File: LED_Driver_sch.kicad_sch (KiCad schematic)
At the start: 32 parts, among them J7 12V IN, J8 12V RGB LED, Q1 PMOS, Q2 NMOS, Q3 NMOS, Q4 NMOS, U6 TLV9001TIDCKR

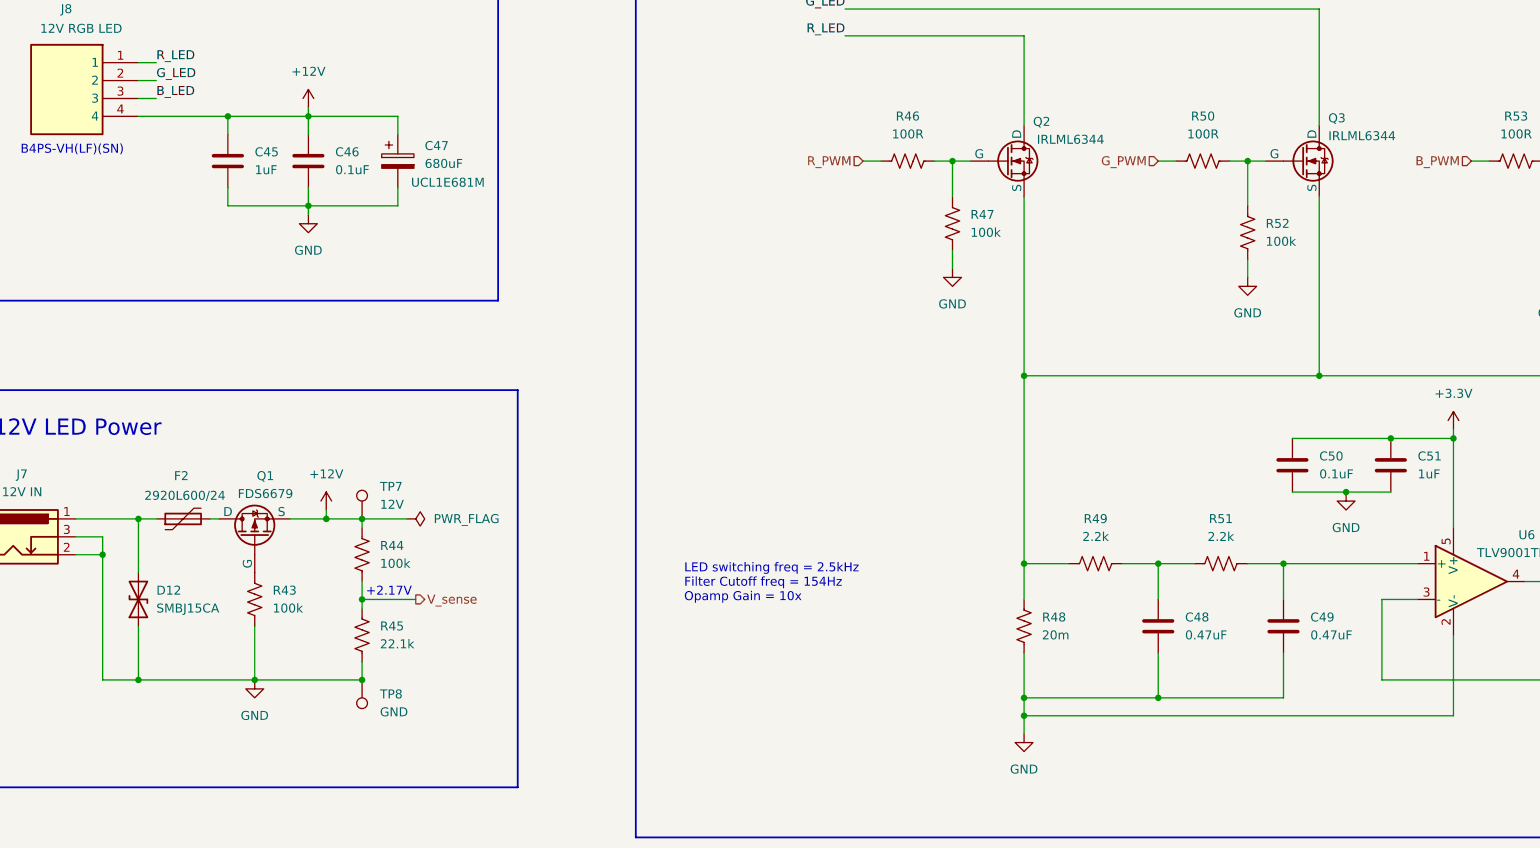
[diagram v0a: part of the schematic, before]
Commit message: Alternate MPNs added
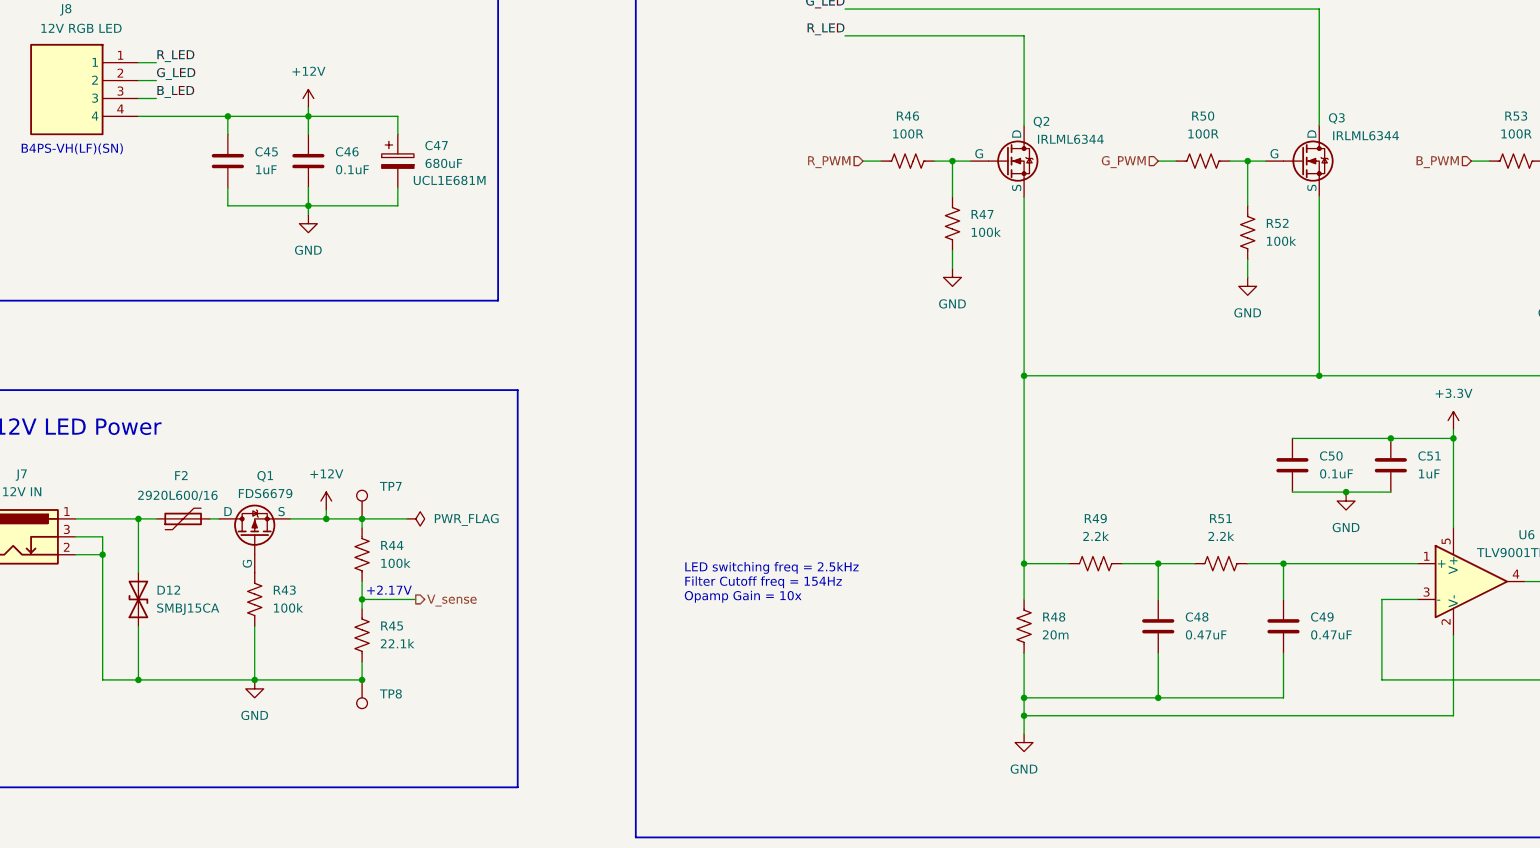
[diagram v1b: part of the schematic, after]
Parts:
- C46: MPN GRM188R71H104KA93D -> C0603C104K5RACTU
- C47: MPN UCL1E681M -> UCL1E681MNL1GS; Manufacturer_Part_Number (none) -> UCL1E681M
- F2: MPN 2920L600/24 -> 2920L600/16MR; Manufacturer_Part_Number (none) -> 2920L600/16
- Q1: MPN FDS6679 -> FDS6679AZ; Manufacturer_Part_Number (none) -> FDS6679
- Q2, Q3, Q4: MPN IRLML6344 -> IRLML6344TRPBF; Manufacturer_Part_Number (none) -> IRLML6344
- TP7: value 12V -> TestPoint
- TP8: value GND -> TestPoint
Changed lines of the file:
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@@
 			)
 		)
-		(property "MPN" "IRLML6344"
+		(property "MPN" "IRLML6344TRPBF"
 			(at 184.404 62.992 0)
 			(effects
@@
 					(color 0 132 132 1)
 				)
+				(hide yes)
 			)
 		)
-		(property "Manufacturer_Part_Number" ""
-			(at 175.26 66.04 0)
+		(property "Manufacturer_Part_Number" "IRLML6344"
+			(at 184.404 62.992 0)
 			(effects
 				(font
 					(size 1.27 1.27)
+					(color 0 132 132 1)
 				)
-				(hide yes)
 			)
 		)
@@
 			)
 		)
-		(property "MPN" "GRM188R71H104KA93D"
+		(property "MPN" "C0603C104K5RACTU"
 			(at 76.2 66.04 0)
 			(effects
@@
 			)
 		)
-		(property "MPN" "IRLML6344"
+		(property "MPN" "IRLML6344TRPBF"
 			(at 220.98 62.484 0)
 			(effects
@@
 				)
 				(justify left)
+				(hide yes)
 			)
 		)
-		(property "Manufacturer_Part_Number" ""
-			(at 217.17 66.04 0)
+		(property "Manufacturer_Part_Number" "IRLML6344"
+			(at 226.314 62.484 0)
 			(effects
 				(font
 					(size 1.27 1.27)
+					(color 0 132 132 1)
 				)
-				(hide yes)
 			)
 		)
@@
 			)
 		)
-		(property "Manufacturer_Part_Number" ""
-			(at 68.58 119.38 90)
+		(property "Manufacturer_Part_Number" "FDS6679"
+			(at 70.104 113.284 90)
 			(effects
 				(font
 					(size 1.27 1.27)
+					(color 0 132 132 1)
 				)
-				(hide yes)
 			)
 		)
-		(property "MPN" "FDS6679"
+		(property "MPN" "FDS6679AZ"
 			(at 70.104 113.284 90)
 			(effects
@@
 					(color 0 132 132 1)
 				)
+				(hide yes)
 			)
 		)
@@
 			)
 		)
-		(property "Value" "12V"
+		(property "Value" "TestPoint"
 			(at 86.36 114.8079 0)
 			(effects
@@
 				)
 				(justify left)
+				(hide yes)
 			)
 		)
@@
 			)
 		)
-		(property "MPN" "UCL1E681M"
+		(property "MPN" "UCL1E681MNL1GS"
 			(at 96.012 69.088 0)
 			(effects
@@
 					(color 0 132 132 1)
 				)
+				(hide yes)
 			)
 		)
@@
 			)
 		)
-		(property "Manufacturer_Part_Number" ""
-			(at 88.9 66.04 0)
+		(property "Manufacturer_Part_Number" "UCL1E681M"
+			(at 96.266 68.834 0)
 			(effects
 				(font
 					(size 1.27 1.27)
+					(color 0 132 132 1)
 				)
-				(hide yes)
 			)
 		)
@@
 			)
 		)
-		(property "Value" "GND"
+		(property "Value" "TestPoint"
 			(at 86.36 144.2719 0)
 			(effects
@@
 				)
 				(justify right)
+				(hide yes)
 			)
 		)
@@
 			)
 		)
-		(property "Description" "PTC RESET FUSE 6.0A 24V 2920"
+		(property "Description" "PTC RESET FUSE 6.0A 16V 2920"
 			(at 58.42 116.84 0)
 			(effects
@@
 			)
 		)
-		(property "MPN" "2920L600/24"
+		(property "MPN" "2920L600/16MR"
 			(at 58.674 113.538 90)
 			(effects
@@
 					(color 0 132 132 1)
 				)
+				(hide yes)
 			)
 		)
@@
 			)
 		)
-		(property "Manufacturer_Part_Number" ""
-			(at 58.42 116.84 90)
+		(property "Manufacturer_Part_Number" "2920L600/16"
+			(at 57.658 113.538 90)
 			(effects
 				(font
 					(size 1.27 1.27)
+					(color 0 132 132 1)
 				)
-				(hide yes)
 			)
 		)
@@
 			)
 		)
-		(property "MPN" "IRLML6344"
+		(property "MPN" "IRLML6344TRPBF"
 			(at 267.97 62.23 0)
 			(effects
@@
 					(color 0 132 132 1)
 				)
+				(hide yes)
 			)
 		)
-		(property "Manufacturer_Part_Number" ""
-			(at 259.08 66.04 0)
+		(property "Manufacturer_Part_Number" "IRLML6344"
+			(at 267.97 62.23 0)
 			(effects
 				(font
 					(size 1.27 1.27)
+					(color 0 132 132 1)
 				)
-				(hide yes)
 			)
 		)

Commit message: SV's comments
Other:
- note added: "Add ESD for 12V - DNP"
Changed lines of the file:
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@@
+		)
+	)
+	(text "Add ESD for 12V - DNP"
+		(exclude_from_sim no)
+		(at 54.102 81.534 0)
+		(effects
+			(font
+				(size 1.27 1.27)
+				(color 255 3 0 1)
+			)
 		)
 	)

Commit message: All comments addressed
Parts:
- added D15: SMBJ15A, footprints:SMBJ15A, symbol SMBJ15A:SMBJ15A
- added D16, D17, D18: SMF15A, Diode_SMD:D_SMF, symbol Diode:SMF15A
- U6: Manufacturer_Part_Number (none) -> TLV9001
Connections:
- net +12V: now also Q1.2 (S), D15.1 (K); no longer Q1.3 (S)
- net B_LED: now also D16.1 (A1)
- net GND: now also D15.2 (A), D16.2 (A2), D17.2 (A2), D18.2 (A2)
- net G_LED: now also D17.1 (A1)
- net R_LED: now also D18.1 (A1)
- net at Q1.1 (G): now also R43.1; no longer F2.2
- new net: F2.2, Q1.3 (D)
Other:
- note removed: "Add ESD for 12V - DNP"
- moved on the sheet: C45, C46, C47
